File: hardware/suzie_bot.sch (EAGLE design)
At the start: 24 parts, among them IC1 LT1529CT33, IC2 L9637DDIP-ADAPTED, Y1 14.7456, Y2 6.0

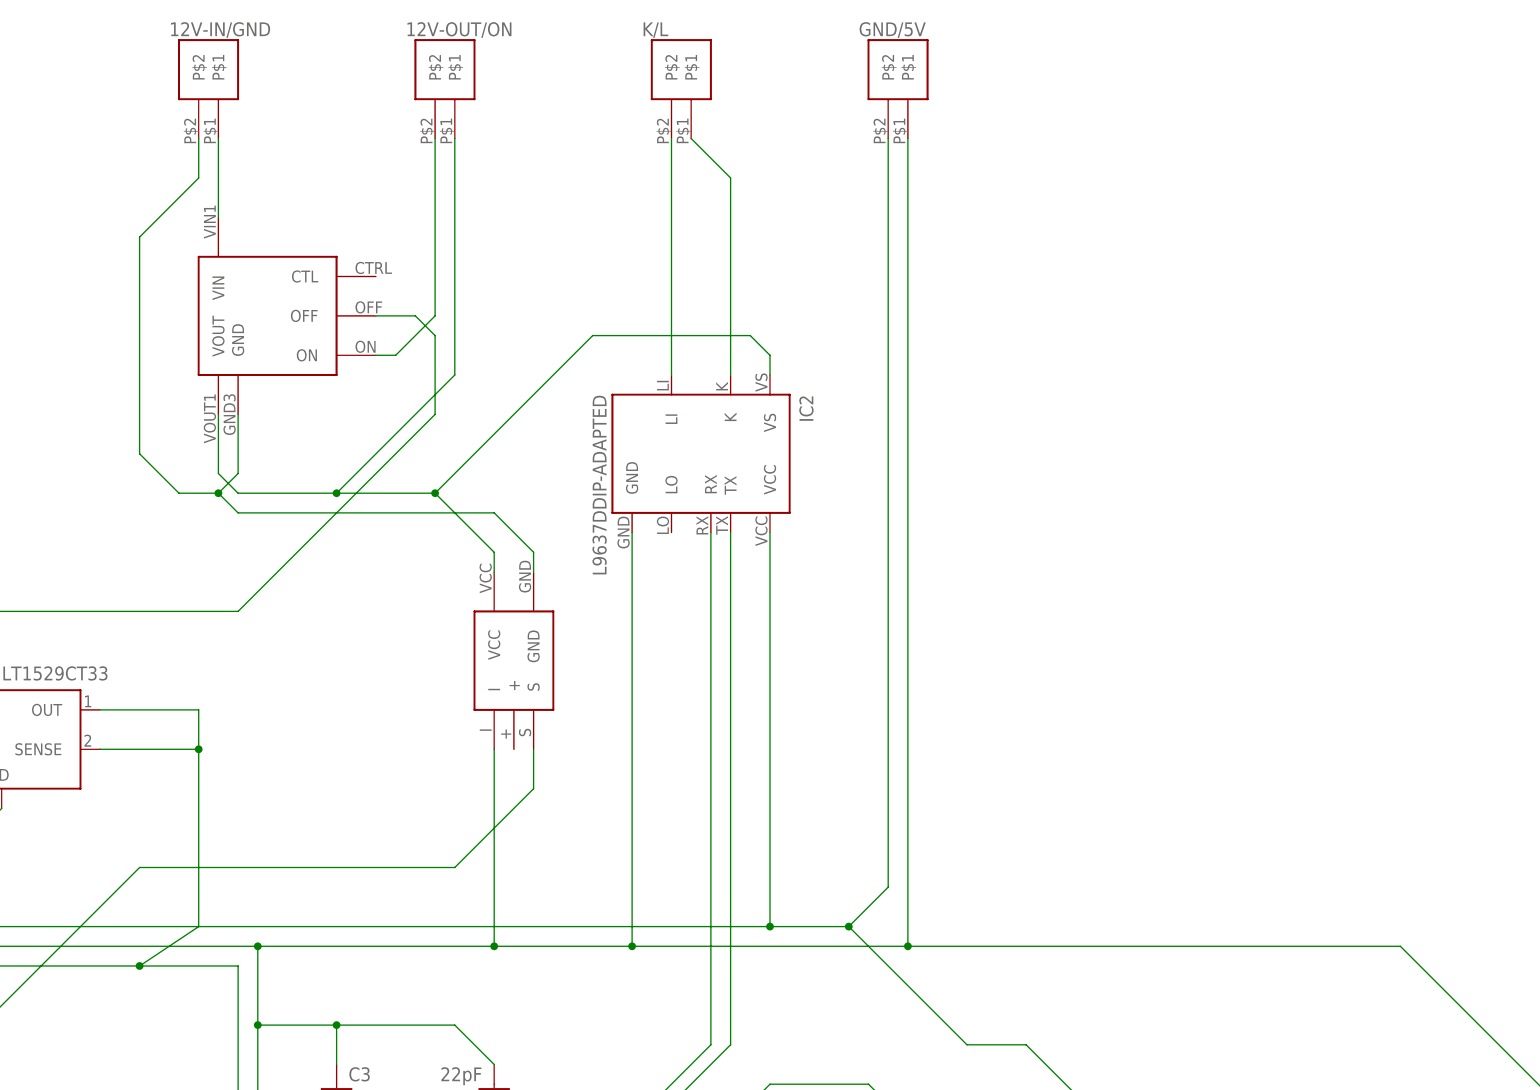
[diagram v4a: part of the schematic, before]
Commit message: Some routing alterations; fixing SD card package sizing.
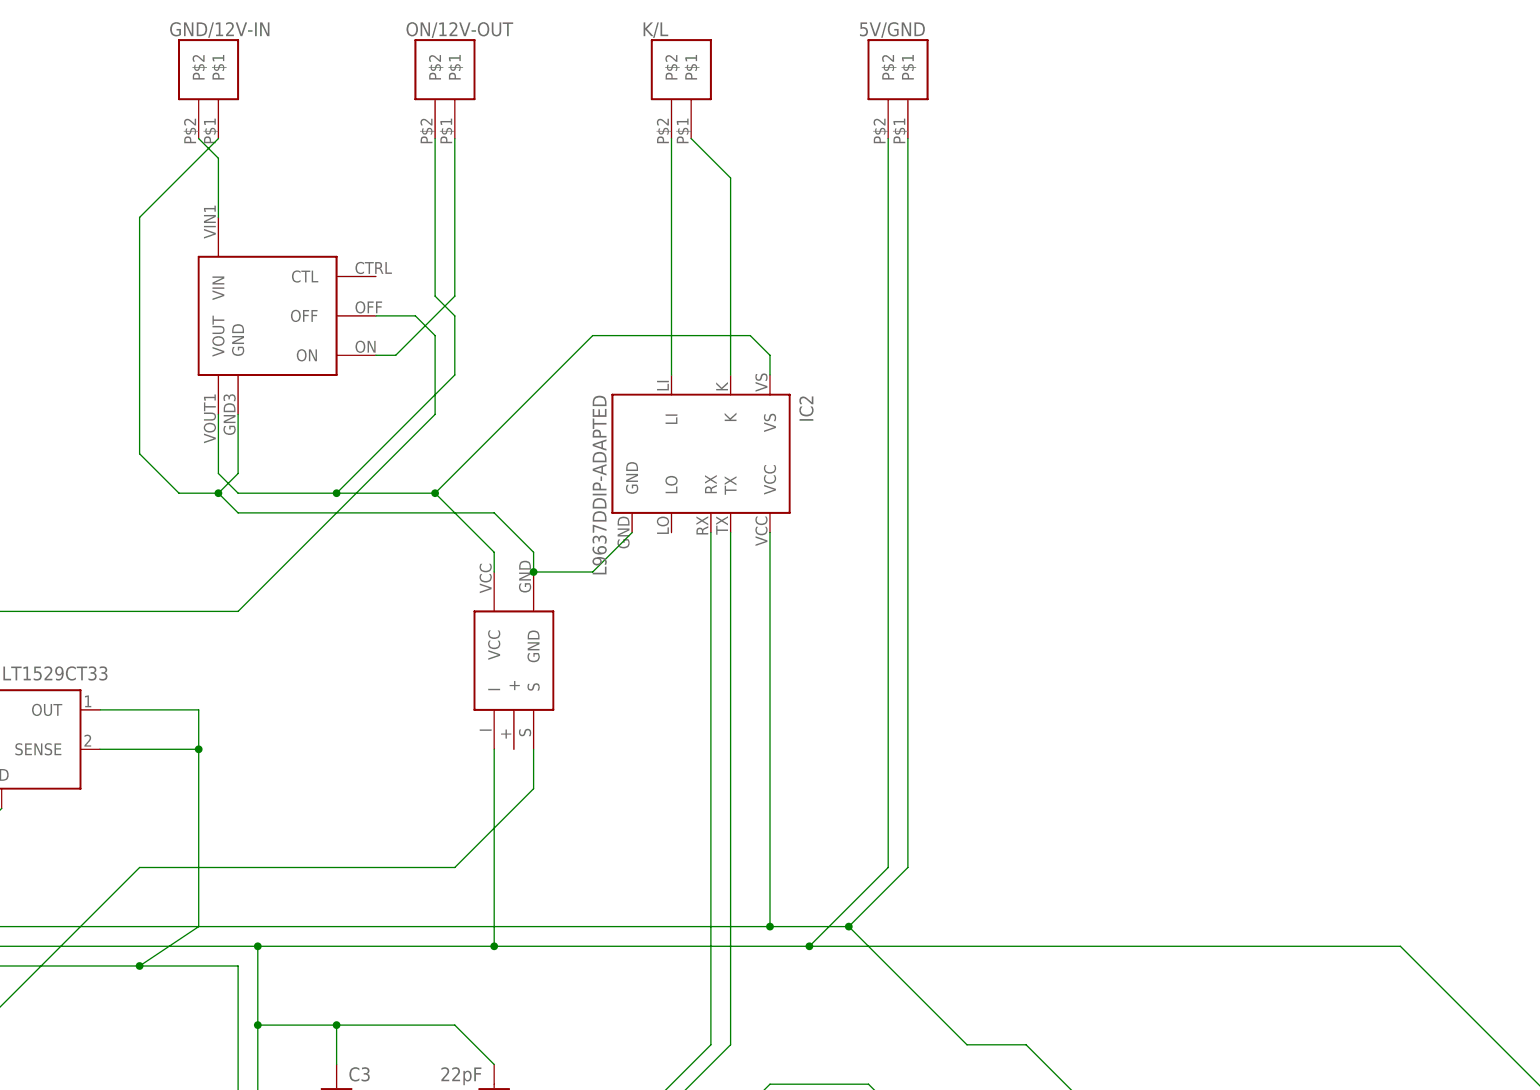
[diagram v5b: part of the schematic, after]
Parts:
- renumbered 12V-IN/GND to GND/12V-IN, 12V-OUT/ON to ON/12V-OUT, GND/5V to 5V/GND
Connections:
- net 12V-OUT: now also ON/12V-OUT.P$2; no longer ON/12V-OUT.P$1
- net 5V: now also 5V/GND.P$1; no longer 5V/GND.P$2
- net EXTGND: now also GND/12V-IN.P$1, IC2.GND; no longer GND/12V-IN.P$2
- net GND: now also 5V/GND.P$2; no longer 5V/GND.P$1, IC2.GND
- net N$7: now also GND/12V-IN.P$2; no longer GND/12V-IN.P$1
- net POWERON: now also ON/12V-OUT.P$1; no longer ON/12V-OUT.P$2
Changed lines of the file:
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@@
 <part name="R2" library="SparkFun-Passives" deviceset="RESISTOR" device="PTH-1/6W" value="1k"/>
 <part name="U$6" library="SparkFun-Boards" deviceset="LOGIC_LEVEL_CONVERTER" device=""/>
-<part name="12V-OUT/ON" library="randomjunk" deviceset="2-PIN-TERMINAL" device=""/>
-<part name="12V-IN/GND" library="randomjunk" deviceset="2-PIN-TERMINAL" device=""/>
+<part name="ON/12V-OUT" library="randomjunk" deviceset="2-PIN-TERMINAL" device=""/>
+<part name="GND/12V-IN" library="randomjunk" deviceset="2-PIN-TERMINAL" device=""/>
 <part name="K/L" library="randomjunk" deviceset="2-PIN-TERMINAL" device=""/>
-<part name="GND/5V" library="randomjunk" deviceset="2-PIN-TERMINAL" device=""/>
+<part name="5V/GND" library="randomjunk" deviceset="2-PIN-TERMINAL" device=""/>
 </parts>
 <sheets>
@@
 <instance part="R2" gate="G$1" x="93.98" y="129.54"/>
 <instance part="U$6" gate="G$1" x="-111.76" y="124.46" rot="MR270"/>
-<instance part="12V-OUT/ON" gate="G$1" x="104.14" y="299.72" rot="R180"/>
-<instance part="12V-IN/GND" gate="G$1" x="73.66" y="299.72" rot="R180"/>
+<instance part="ON/12V-OUT" gate="G$1" x="104.14" y="299.72" rot="R180"/>
+<instance part="GND/12V-IN" gate="G$1" x="73.66" y="299.72" rot="R180"/>
 <instance part="K/L" gate="G$1" x="134.62" y="299.72" rot="R180"/>
-<instance part="GND/5V" gate="G$1" x="162.56" y="299.72" rot="R180"/>
+<instance part="5V/GND" gate="G$1" x="162.56" y="299.72" rot="R180"/>
 </instances>
 <busses>
@@
 <wire x1="-45.72" y1="142.24" x2="-45.72" y2="198.12" width="0.1524" layer="91"/>
 <wire x1="-45.72" y1="198.12" x2="20.32" y2="198.12" width="0.1524" layer="91"/>
-<wire x1="154.94" y1="198.12" x2="160.02" y2="203.2" width="0.1524" layer="91"/>
+<wire x1="154.94" y1="198.12" x2="162.56" y2="205.74" width="0.1524" layer="91"/>
 <junction x="154.94" y="198.12"/>
-<pinref part="GND/5V" gate="G$1" pin="P$2"/>
-<wire x1="160.02" y1="203.2" x2="160.02" y2="299.72" width="0.1524" layer="91"/>
+<pinref part="5V/GND" gate="G$1" pin="P$1"/>
+<wire x1="162.56" y1="299.72" x2="162.56" y2="205.74" width="0.1524" layer="91"/>
 </segment>
 </net>
@@
 <wire x1="76.2" y1="254" x2="88.9" y2="254" width="0.1524" layer="91"/>
 <wire x1="88.9" y1="254" x2="104.14" y2="269.24" width="0.1524" layer="91"/>
-<pinref part="12V-OUT/ON" gate="G$1" pin="P$1"/>
-<wire x1="104.14" y1="269.24" x2="104.14" y2="299.72" width="0.1524" layer="91"/>
 <pinref part="U$10" gate="G$1" pin="VCC"/>
 <wire x1="109.22" y1="243.84" x2="109.22" y2="246.38" width="0.1524" layer="91"/>
@@
 <wire x1="144.78" y1="271.78" x2="144.78" y2="269.24" width="0.1524" layer="91"/>
 <wire x1="121.92" y1="274.32" x2="142.24" y2="274.32" width="0.1524" layer="91"/>
+<pinref part="ON/12V-OUT" gate="G$1" pin="P$2"/>
+<wire x1="101.6" y1="299.72" x2="101.6" y2="279.4" width="0.1524" layer="91"/>
+<wire x1="101.6" y1="279.4" x2="104.14" y2="276.86" width="0.1524" layer="91"/>
+<wire x1="104.14" y1="276.86" x2="104.14" y2="269.24" width="0.1524" layer="91"/>
 </segment>
 </net>
@@
 <pinref part="U$4" gate="G$1" pin="ON"/>
 <wire x1="93.98" y1="271.78" x2="96.52" y2="271.78" width="0.1524" layer="91"/>
-<wire x1="96.52" y1="271.78" x2="101.6" y2="276.86" width="0.1524" layer="91"/>
-<pinref part="12V-OUT/ON" gate="G$1" pin="P$2"/>
-<wire x1="101.6" y1="276.86" x2="101.6" y2="299.72" width="0.1524" layer="91"/>
+<wire x1="96.52" y1="271.78" x2="104.14" y2="279.4" width="0.1524" layer="91"/>
+<pinref part="ON/12V-OUT" gate="G$1" pin="P$1"/>
+<wire x1="104.14" y1="299.72" x2="104.14" y2="279.4" width="0.1524" layer="91"/>
 </segment>
 </net>
@@
 <pinref part="K/L" gate="G$1" pin="P$2"/>
 <wire x1="132.08" y1="269.24" x2="132.08" y2="299.72" width="0.1524" layer="91"/>
-</segment>
-</net>
-<net name="N$7" class="1">
-<segment>
-<pinref part="U$4" gate="G$1" pin="VIN"/>
-<pinref part="12V-IN/GND" gate="G$1" pin="P$1"/>
-<wire x1="73.66" y1="299.72" x2="73.66" y2="289.56" width="0.1524" layer="91"/>
 </segment>
 </net>
@@
 <wire x1="22.86" y1="195.58" x2="78.74" y2="195.58" width="0.1524" layer="91"/>
 <wire x1="78.74" y1="195.58" x2="109.22" y2="195.58" width="0.1524" layer="91"/>
-<wire x1="109.22" y1="195.58" x2="127" y2="195.58" width="0.1524" layer="91"/>
-<pinref part="IC2" gate="G$1" pin="GND"/>
-<wire x1="127" y1="248.92" x2="127" y2="195.58" width="0.1524" layer="91"/>
-<junction x="127" y="195.58"/>
 <wire x1="-50.8" y1="195.58" x2="-127" y2="195.58" width="0.1524" layer="91"/>
 <wire x1="-127" y1="195.58" x2="-144.78" y2="195.58" width="0.1524" layer="91"/>
 <wire x1="-144.78" y1="195.58" x2="-182.88" y2="195.58" width="0.1524" layer="91"/>
-<wire x1="127" y1="195.58" x2="162.56" y2="195.58" width="0.1524" layer="91"/>
 <pinref part="U$9" gate="G$1" pin="GND"/>
-<wire x1="162.56" y1="195.58" x2="226.06" y2="195.58" width="0.1524" layer="91"/>
+<wire x1="109.22" y1="195.58" x2="149.86" y2="195.58" width="0.1524" layer="91"/>
+<wire x1="149.86" y1="195.58" x2="226.06" y2="195.58" width="0.1524" layer="91"/>
 <wire x1="228.6" y1="137.16" x2="233.68" y2="132.08" width="0.1524" layer="91"/>
 <wire x1="233.68" y1="132.08" x2="241.3" y2="132.08" width="0.1524" layer="91"/>
@@
 <wire x1="-137.16" y1="93.98" x2="-149.86" y2="106.68" width="0.1524" layer="91"/>
 <junction x="-149.86" y="106.68"/>
-<pinref part="GND/5V" gate="G$1" pin="P$1"/>
-<junction x="162.56" y="195.58"/>
-<wire x1="162.56" y1="299.72" x2="162.56" y2="195.58" width="0.1524" layer="91"/>
+<wire x1="149.86" y1="195.58" x2="160.02" y2="205.74" width="0.1524" layer="91"/>
+<junction x="149.86" y="195.58"/>
+<pinref part="5V/GND" gate="G$1" pin="P$2"/>
+<wire x1="160.02" y1="205.74" x2="160.02" y2="299.72" width="0.1524" layer="91"/>
 </segment>
 </net>
@@
 <wire x1="73.66" y1="254" x2="76.2" y2="251.46" width="0.1524" layer="91"/>
 <junction x="73.66" y="254"/>
-<pinref part="12V-IN/GND" gate="G$1" pin="P$2"/>
-<wire x1="71.12" y1="299.72" x2="71.12" y2="294.64" width="0.1524" layer="91"/>
-<wire x1="71.12" y1="294.64" x2="63.5" y2="287.02" width="0.1524" layer="91"/>
-<wire x1="63.5" y1="287.02" x2="63.5" y2="259.08" width="0.1524" layer="91"/>
+<wire x1="63.5" y1="289.56" x2="63.5" y2="259.08" width="0.1524" layer="91"/>
 <wire x1="63.5" y1="259.08" x2="68.58" y2="254" width="0.1524" layer="91"/>
 <wire x1="68.58" y1="254" x2="73.66" y2="254" width="0.1524" layer="91"/>
-</segment>
-</net>
+<pinref part="GND/12V-IN" gate="G$1" pin="P$1"/>
+<wire x1="73.66" y1="299.72" x2="63.5" y2="289.56" width="0.1524" layer="91"/>
+<pinref part="IC2" gate="G$1" pin="GND"/>
+<wire x1="114.3" y1="243.84" x2="121.92" y2="243.84" width="0.1524" layer="91"/>
+<wire x1="121.92" y1="243.84" x2="127" y2="248.92" width="0.1524" layer="91"/>
+<junction x="114.3" y="243.84"/>
+</segment>
+</net>
+<net name="N$7" class="0">
+<segment>
+<pinref part="U$4" gate="G$1" pin="VIN"/>
+<pinref part="GND/12V-IN" gate="G$1" pin="P$2"/>
+<wire x1="73.66" y1="289.56" x2="73.66" y2="297.18" width="0.1524" layer="91"/>
+<wire x1="73.66" y1="297.18" x2="71.12" y2="299.72" width="0.1524" layer="91"/>
+</segment>
+</net>
